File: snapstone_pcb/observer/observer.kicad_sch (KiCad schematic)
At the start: 1 part, among them U1 ZRE200GE_Motion_Sensor

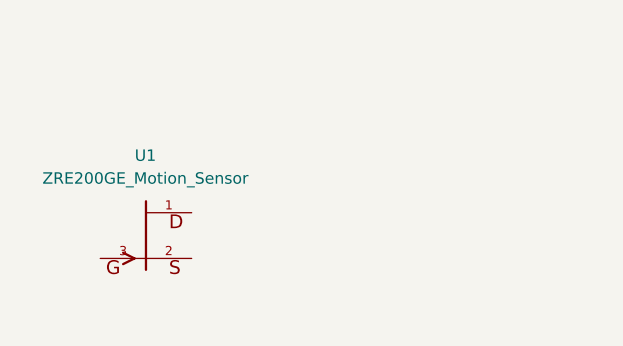
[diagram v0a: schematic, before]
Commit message: Made part files project-specific, implemented battery holder in redstone block, moved .pretty file under redstone_repeater/ to part_files/, implemented analog switch & motion sensor in observer schematic
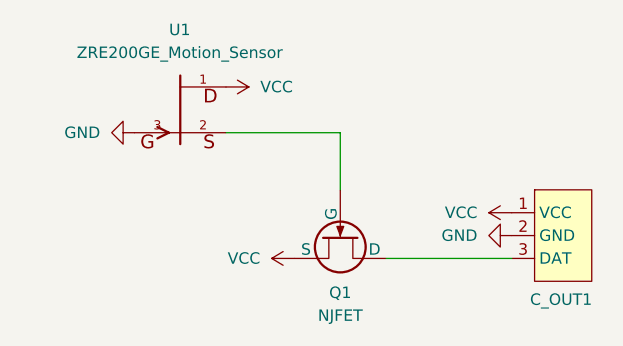
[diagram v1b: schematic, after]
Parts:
- added C_OUT1: ~, 691137710003_Board_To_Wire:691137710003_Board_To_Wire, symbol snapstone:3_Pin_Block_Connector
- added Q1: NJFET, symbol Simulation_SPICE:NJFET
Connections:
- net VCC: now reaches U1.1
- net VCC: now also C_OUT1.1 (VCC), Q1.3 (S)
- net at U1.2: now also Q1.2 (G)
- net GND: now reaches U1.3
- net GND: now also C_OUT1.2 (GND)
- new net: C_OUT1.3 (DAT), Q1.1 (D)
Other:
- moved on the sheet: U1

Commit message: did a bunch of stuff (something something Redstone Repeater PCB Changes)
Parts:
- C_OUT1: value ~ -> (none)
- Q1: footprint (none) -> MMBFJ112_Analog_Switch:SOT-23_ONS

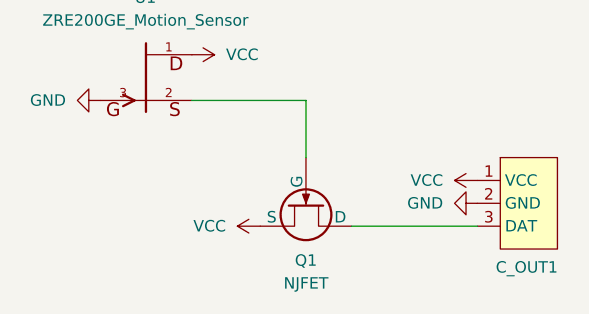
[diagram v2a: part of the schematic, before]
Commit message: Replaced JFET switch part with different model (MMBFJ270_Analog_Switch)
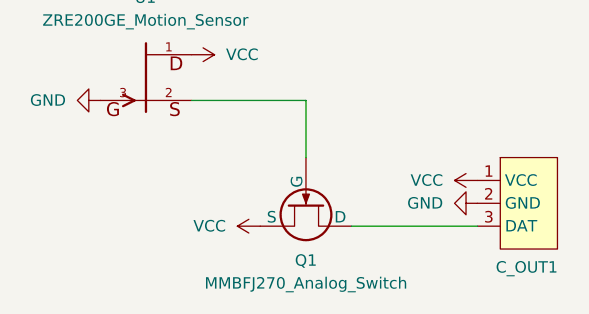
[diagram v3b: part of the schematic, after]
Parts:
- Q1: value NJFET -> MMBFJ270_Analog_Switch; footprint MMBFJ112_Analog_Switch:SOT-23_ONS -> MMBFJ270_Analog_Switch:SOT-23_ONS
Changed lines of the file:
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@@
 			)
 		)
-		(property "Value" "NJFET"
+		(property "Value" "MMBFJ270_Analog_Switch"
 			(at 120.65 104.14 90)
 			(show_name no)
@@
 			)
 		)
-		(property "Footprint" "MMBFJ112_Analog_Switch:SOT-23_ONS"
+		(property "Footprint" "MMBFJ270_Analog_Switch:SOT-23_ONS"
 			(at 123.19 100.33 0)
 			(hide yes)

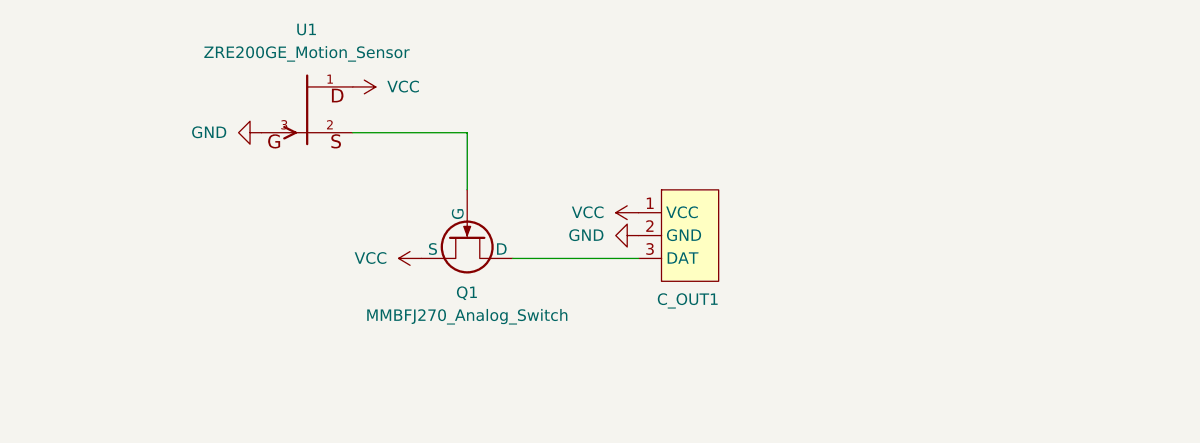
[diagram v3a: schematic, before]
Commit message: Updated resistor footprint project-wide
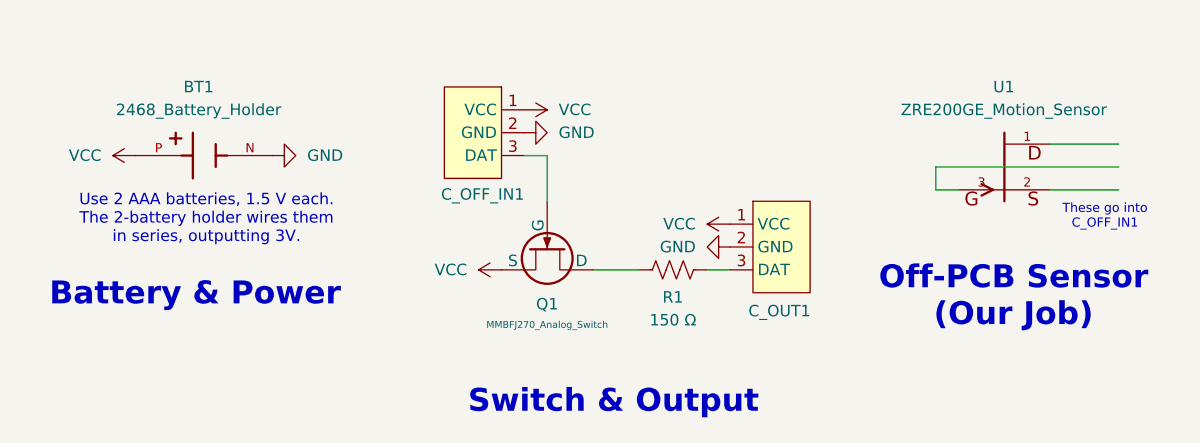
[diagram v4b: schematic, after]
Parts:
- added BT1: 2468_Battery_Holder, 2468_Battery_Holder:BAT_2468, symbol 2468_Battery_Holder:2468
- added C_OFF_IN1: (no value), 691137710003_Board_To_Wire:691137710003_Board_To_Wire, symbol snapstone:3_Pin_Block_Connector
- added R1: 150 Ω, CF12JT_Resistor:STA_CF12_STP, symbol Device:R_US
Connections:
- net GND: now also BT1.N, C_OFF_IN1.2 (GND); no longer U1.3
- net VCC: now also BT1.P, C_OFF_IN1.1 (VCC); no longer U1.1
- net at C_OUT1.3 (DAT): now also R1.1; no longer Q1.1 (D)
- net at U1.2: no longer Q1.2 (G)
- new net: Q1.1 (D), R1.2
- new net: C_OFF_IN1.3 (DAT), Q1.2 (G)
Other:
- note added: "Battery & Power"
- note added: "Off-PCB Sensor (Our Job)"
- note added: "Switch & Output"
- note added: "These go into C_OFF_IN1"
- note added: "Use 2 AAA batteries, 1.5 V each. The 2-battery holder wires them in series, outputting 3V."
- moved on the sheet: C_OUT1, Q1
